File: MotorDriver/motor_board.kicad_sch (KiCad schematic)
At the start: 76 parts, among them J1 Conn_01x04_Socket, J10 Conn_01x04_Socket, J2 Conn_01x03_Pin, J3 Conn_01x03_Pin, J4 Screw_Terminal_01x02, J5 Screw_Terminal_01x04, J6 Screw_Terminal_01x04, J7 Conn_01x16_Socket, J8 Conn_01x16_Socket, J9 Conn_01x16_Socket, Q1 AON6411, U1 PCA9685PW, U2 TB6612FNG, U3 TB6612FNG

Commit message: v2 of the motor driver
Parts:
- removed D1: LED, LED_SMD:LED_0805_2012Metric_Pad1.15x1.40mm_HandSolder, symbol Device:LED
- removed J2, J3: Conn_01x03_Pin, Connector_PinHeader_2.54mm:PinHeader_1x03_P2.54mm_Vertical, symbol Connector:Conn_01x03_Pin
- removed R8: 300, Resistor_SMD:R_0805_2012Metric_Pad1.20x1.40mm_HandSolder, symbol Device:R
- removed TP1, TP2, TP3, TP4, TP5: TestPoint, TestPoint:TestPoint_Pad_D2.0mm, symbol Connector:TestPoint
- H1, H2, H3, H4: footprint MountingHole:MountingHole_3.2mm_M3 -> MountingHole:MountingHole_2.5mm
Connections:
- net SERVO is gone; now on net +12V: J8.1 (Pin_1), J8.2 (Pin_2), J8.3 (Pin_3), J8.4 (Pin_4), J8.5 (Pin_5), J8.6 (Pin_6)
- net SERVO1 is gone; now on net +12V: J8.10 (Pin_10), J8.11 (Pin_11), J8.12 (Pin_12), J8.7 (Pin_7), J8.8 (Pin_8), J8.9 (Pin_9)
- net Vmot1 is gone; now on net +12V: U3.13 (VM2), U3.14 (VM3), U3.24 (VM1)
- net Vmot2 is gone; now on net +12V: U2.13 (VM2), U2.14 (VM3), U2.24 (VM1)
- net GND: now also J4.1 (Pin_1); no longer J4.2 (Pin_2)
- net M1A: now also U3.1 (AO1), U3.2 (AO1); no longer U2.1 (AO1), U2.2 (AO1)
- net M1B: now also U3.5 (AO2), U3.6 (AO2); no longer U2.5 (AO2), U2.6 (AO2)
- net M2A: now also U3.7 (BO2), U3.8 (BO2); no longer U2.7 (BO2), U2.8 (BO2)
- net M2B: now also U3.11 (BO1), U3.12 (BO1); no longer U2.11 (BO1), U2.12 (BO1)
- net M3A: now also U2.1 (AO1), U2.2 (AO1); no longer U3.1 (AO1), U3.2 (AO1)
- net M3B: now also U2.5 (AO2), U2.6 (AO2); no longer U3.5 (AO2), U3.6 (AO2)
- net M4A: now also U2.7 (BO2), U2.8 (BO2); no longer U3.7 (BO2), U3.8 (BO2)
- net M4B: now also U2.11 (BO1), U2.12 (BO1); no longer U3.11 (BO1), U3.12 (BO1)
- net PWM0: now also J7.1 (Pin_1); no longer J7.15 (Pin_15)
- net PWM1: now also J7.2 (Pin_2); no longer J7.16 (Pin_16)
- net PWM10: now also J7.11 (Pin_11); no longer J7.9 (Pin_9)
- net PWM11: now also J7.12 (Pin_12); no longer J7.10 (Pin_10)
- net PWM12: now also J7.13 (Pin_13); no longer J7.11 (Pin_11)
- net PWM13: now also J7.14 (Pin_14); no longer J7.12 (Pin_12)
- net PWM14: now also J7.15 (Pin_15); no longer J7.13 (Pin_13)
- net PWM15: now also J7.16 (Pin_16); no longer J7.14 (Pin_14)
- net PWM2: now also J7.3 (Pin_3); no longer J7.1 (Pin_1)
- net PWM3: now also J7.4 (Pin_4); no longer J7.2 (Pin_2)
- net PWM4: now also J7.5 (Pin_5); no longer J7.3 (Pin_3)
- net PWM5: now also J7.6 (Pin_6); no longer J7.4 (Pin_4)
- net PWM6: now also J7.7 (Pin_7); no longer J7.5 (Pin_5)
- net PWM7: now also J7.8 (Pin_8); no longer J7.6 (Pin_6)
- net PWM8: now also J7.9 (Pin_9); no longer J7.7 (Pin_7)
- net PWM9: now also J7.10 (Pin_10); no longer J7.8 (Pin_8)
- net at Q1.5 (D): now also J4.2 (Pin_2); no longer J4.1 (Pin_1)
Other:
- note removed: "Voltage selector"
- moved on the sheet: C1, C2, C3, C4, C5, J1, J10, J4, Q1

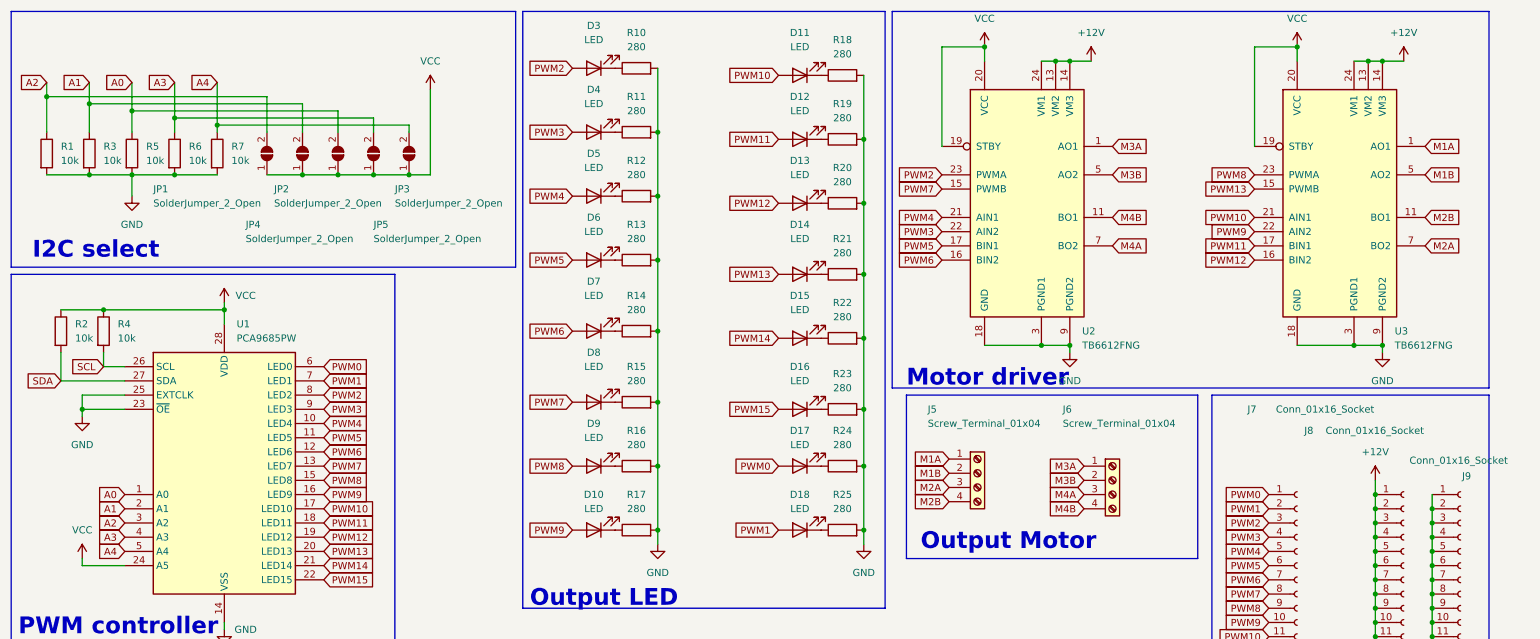
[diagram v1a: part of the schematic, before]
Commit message: update motor driver
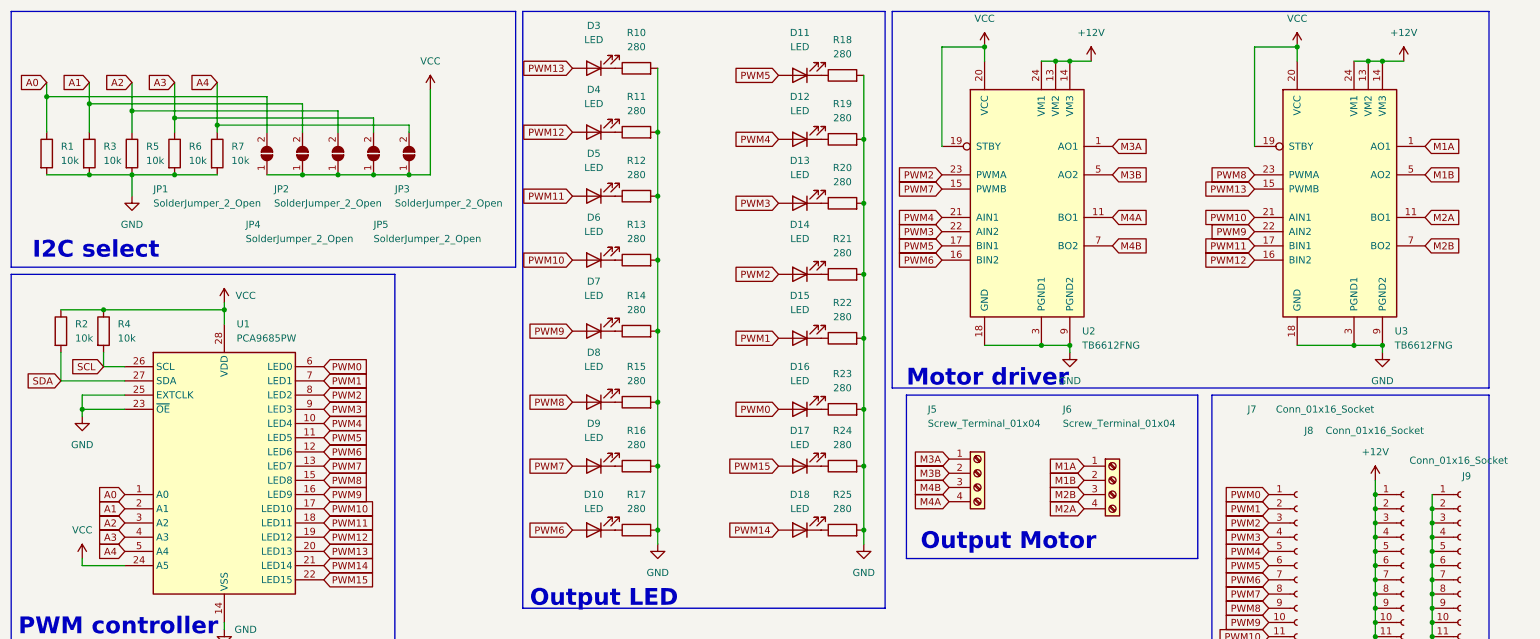
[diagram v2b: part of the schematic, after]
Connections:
- net A0: now also JP1.2 (B), R1.1; no longer JP3.2 (B), R5.1
- net A2: now also JP3.2 (B), R5.1; no longer JP1.2 (B), R1.1
- net M1A: now also J6.1 (Pin_1); no longer J5.1 (Pin_1)
- net M1B: now also J6.2 (Pin_2); no longer J5.2 (Pin_2)
- net M2A: now also J6.4 (Pin_4), U3.11 (BO1), U3.12 (BO1); no longer J5.3 (Pin_3), U3.7 (BO2), U3.8 (BO2)
- net M2B: now also J6.3 (Pin_3), U3.7 (BO2), U3.8 (BO2); no longer J5.4 (Pin_4), U3.11 (BO1), U3.12 (BO1)
- net M3A: now also J5.1 (Pin_1); no longer J6.1 (Pin_1)
- net M3B: now also J5.2 (Pin_2); no longer J6.2 (Pin_2)
- net M4A: now also J5.4 (Pin_4), U2.11 (BO1), U2.12 (BO1); no longer J6.3 (Pin_3), U2.7 (BO2), U2.8 (BO2)
- net M4B: now also J5.3 (Pin_3), U2.7 (BO2), U2.8 (BO2); no longer J6.4 (Pin_4), U2.11 (BO1), U2.12 (BO1)
- net PWM0: now also D16.2 (A); no longer D17.2 (A)
- net PWM1: now also D15.2 (A); no longer D18.2 (A)
- net PWM10: now also D6.2 (A); no longer D11.2 (A)
- net PWM11: now also D5.2 (A); no longer D12.2 (A)
- net PWM12: now also D4.2 (A); no longer D13.2 (A)
- net PWM13: now also D3.2 (A); no longer D14.2 (A)
- net PWM14: now also D18.2 (A); no longer D15.2 (A)
- net PWM15: now also D17.2 (A); no longer D16.2 (A)
- net PWM2: now also D14.2 (A); no longer D3.2 (A)
- net PWM3: now also D13.2 (A); no longer D4.2 (A)
- net PWM4: now also D12.2 (A); no longer D5.2 (A)
- net PWM5: now also D11.2 (A); no longer D6.2 (A)
- net PWM6: now also D10.2 (A); no longer D7.2 (A)
- net PWM7: now also D9.2 (A); no longer D8.2 (A)
- net PWM8: now also D8.2 (A); no longer D9.2 (A)
- net PWM9: now also D7.2 (A); no longer D10.2 (A)

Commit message: added IMU
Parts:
- removed R25: 280, Resistor_SMD:R_0805_2012Metric_Pad1.20x1.40mm_HandSolder, symbol Device:R
- added CR1: MBR120VLSFT1G, MBR120:SDO_SOD-123FL_ONS, symbol 2025-03-26_09-20-52:MBR120VLSFT1G
- added D1, D19, D20, D21, D22, D23, D24, D25, D26, D27, D28, D29, D30, D31, D32, D33: 1N4148W, Diode_SMD:D_SOD-123, symbol Diode:1N4148W
- added J3: Conn_01x02_Socket, Connector_PinHeader_2.54mm:PinHeader_1x02_P2.54mm_Vertical, symbol Connector:Conn_01x02_Socket
- added R26: 1k1, Resistor_SMD:R_0805_2012Metric_Pad1.20x1.40mm_HandSolder, symbol Device:R
- added R27: 3k9, Resistor_SMD:R_0805_2012Metric_Pad1.20x1.40mm_HandSolder, symbol Device:R
- added R8: 270, Resistor_SMD:R_0805_2012Metric, symbol Device:R
- added SW9: SW_Push, Button_Switch_SMD:SW_Push_SPST_NO_Alps_SKRK, symbol Switch:SW_Push
- added U4: AMS1117, Package_TO_SOT_SMD:SOT-223-3_TabPin2, symbol Regulator_Linear:AMS1117
- R10, R11, R12, R13, R14, R15, R16, R17, R18, R19, R20, R21, R22, R23, R24: value 280 -> 270; footprint Resistor_SMD:R_0805_2012Metric_Pad1.20x1.40mm_HandSolder -> Resistor_SMD:R_0805_2012Metric
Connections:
- net +12V: now also CR1.2, R27.2
- net GND: now also J3.1 (Pin_1), R26.1, R8.2, U4.1 (ADJ)
- net PWM10: now also D28.2 (A); no longer D6.2 (A), J7.11 (Pin_11), U3.21 (AIN1)
- net PWM11: now also D30.2 (A); no longer D5.2 (A), J7.12 (Pin_12), U3.17 (BIN1)
- net PWM13: now also D32.2 (A); no longer D3.2 (A), J7.14 (Pin_14), U3.15 (PWMB)
- net PWM2: now also D1.2 (A); no longer D14.2 (A), J7.3 (Pin_3), U2.23 (PWMA)
- net PWM4: now also D21.2 (A); no longer D12.2 (A), J7.5 (Pin_5), U2.21 (AIN1)
- net PWM5: now also D22.2 (A); no longer D11.2 (A), J7.6 (Pin_6), U2.17 (BIN1)
- net PWM7: now also D24.2 (A); no longer D9.2 (A), J7.8 (Pin_8), U2.15 (PWMB)
- net PWM8: now also D26.2 (A); no longer D8.2 (A), J7.9 (Pin_9), U3.23 (PWMA)
- net VCC: now also SW9.1, U4.2 (VO)
- net at D13.1 (K): now also R19.1; no longer R20.1
- net at D10.1 (K): now also R16.1; no longer R17.1
- net at D3.1 (K): now also R8.1; no longer R10.1
- net at D9.1 (K): now also R15.1; no longer R16.1
- net at R12.1: now also D6.1 (K); no longer D5.1 (K)
- net at D12.1 (K): now also R18.1; no longer R19.1
- net at D7.1 (K): now also R13.1; no longer R14.1
- net at D16.1 (K): now also R22.1; no longer R23.1
- net at D15.1 (K): now also R21.1; no longer R22.1
- net at R11.1: now also D5.1 (K); no longer D4.1 (K)
- net at D18.1 (K): now also R24.1
- net at D17.1 (K): now also R23.1; no longer R24.1
- net at D8.1 (K): now also R14.1; no longer R15.1
- net at D14.1 (K): now also R20.1; no longer R21.1
- net at D11.1 (K): now also R17.1; no longer R18.1
- new net: J3.2 (Pin_2), R26.2, R27.1
- new net: CR1.1, U4.3 (VI)
- new net: D4.1 (K), R10.1
- new net PWM10motor: D28.1 (K), D29.1 (K), D6.2 (A), J7.11 (Pin_11), U3.21 (AIN1)
- new net PWM11motor: D30.1 (K), D31.1 (K), D5.2 (A), J7.12 (Pin_12), U3.17 (BIN1)
- new net PWM13motor: D3.2 (A), D32.1 (K), D33.1 (K), J7.14 (Pin_14), U3.15 (PWMB)
- new net PWM2motor: D1.1 (K), D14.2 (A), D19.1 (K), J7.3 (Pin_3), U2.23 (PWMA)
- new net PWM4motor: D12.2 (A), D20.1 (K), D21.1 (K), J7.5 (Pin_5), U2.21 (AIN1)
- new net PWM5motor: D11.2 (A), D22.1 (K), D23.1 (K), J7.6 (Pin_6), U2.17 (BIN1)
- new net PWM7motor: D24.1 (K), D25.1 (K), D9.2 (A), J7.8 (Pin_8), U2.15 (PWMB)
- new net PWM8motor: D26.1 (K), D27.1 (K), D8.2 (A), J7.9 (Pin_9), U3.23 (PWMA)
- new net testvoltage: D19.2 (A), D20.2 (A), D23.2 (A), D25.2 (A), D27.2 (A), D29.2 (A), D31.2 (A), D33.2 (A), SW9.2
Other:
- added sheet overflow (overflow.kicad_sch)
- moved on the sheet: C1, C2, C3, C4, C5, D2, H1, H2, H3, H4, J1, J10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
